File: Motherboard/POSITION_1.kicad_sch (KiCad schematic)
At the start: 28 parts, among them Q1 MOSFET_N_(DMN61D8LQ-13), Q3 MOSFET_N_(ZVN3320FTA)

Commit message: Schematic ready.  Going to clean up directory now.
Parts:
- C13, C14, C15, C20, C21: footprint Capacitors_SMD:C_1206 -> Capacitor_SMD:C_1206_3216Metric
- CAL2: footprint (none) -> Smart_Tank:FEMALE_SPADE_QC_(TE_63969-1)
- CTRL_SHUNT_1, PUMP_SHUNT_1: footprint _GARRETTS_PARTS:SHUNT_(WSL40261L000FEA) -> Smart_Tank:SHUNT_(WSL40261L000FEA)
- D1, D15: footprint Diodes_SMD:SOD-123 -> Diode_SMD:D_SMA
- Q1: footprint Package_TO_SOT_SMD:SOT-23 -> Smart_Tank:SOT-23
- Q3: footprint TO_SOT_Packages_SMD:SOT-23 -> Smart_Tank:SOT-23
- R1, R17, R18, R47, R48, R5, R6, R7: footprint Resistors_SMD:R_1206 -> Resistor_SMD:R_1206_3216Metric
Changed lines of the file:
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@@
 			)
 		)
-		(property "Footprint" "TO_SOT_Packages_SMD:SOT-23"
+		(property "Footprint" "Smart_Tank:SOT-23"
 			(at 119.38 94.615 0)
 			(effects
@@
 			)
 		)
-		(property "Footprint" "Resistors_SMD:R_1206"
+		(property "Footprint" "Resistor_SMD:R_1206_3216Metric"
 			(at 101.6 92.202 90)
 			(effects
@@
 			)
 		)
-		(property "Footprint" "Resistors_SMD:R_1206"
+		(property "Footprint" "Resistor_SMD:R_1206_3216Metric"
 			(at 117.348 81.28 90)
 			(effects
@@
 			)
 		)
-		(property "Footprint" "Resistors_SMD:R_1206"
+		(property "Footprint" "Resistor_SMD:R_1206_3216Metric"
 			(at 94.488 99.06 90)
 			(effects
@@
 			)
 		)
-		(property "Footprint" "Resistors_SMD:R_1206"
+		(property "Footprint" "Resistor_SMD:R_1206_3216Metric"
 			(at 85.09 153.162 90)
 			(effects
@@
 			)
 		)
-		(property "Footprint" "Resistors_SMD:R_1206"
+		(property "Footprint" "Resistor_SMD:R_1206_3216Metric"
 			(at 95.758 160.02 90)
 			(effects
@@
 			)
 		)
-		(property "Footprint" "Capacitors_SMD:C_1206"
+		(property "Footprint" "Capacitor_SMD:C_1206_3216Metric"
 			(at 229.5652 53.34 0)
 			(effects
@@
 			)
 		)
-		(property "Footprint" "Capacitors_SMD:C_1206"
+		(property "Footprint" "Capacitor_SMD:C_1206_3216Metric"
 			(at 219.4052 53.34 0)
 			(effects
@@
 			)
 		)
-		(property "Footprint" "Capacitors_SMD:C_1206"
+		(property "Footprint" "Capacitor_SMD:C_1206_3216Metric"
 			(at 229.5652 139.7 0)
 			(effects
@@
 			)
 		)
-		(property "Footprint" "Capacitors_SMD:C_1206"
+		(property "Footprint" "Capacitor_SMD:C_1206_3216Metric"
 			(at 219.4052 139.7 0)
 			(effects
@@
 			)
 		)
-		(property "Footprint" "Resistors_SMD:R_1206"
+		(property "Footprint" "Resistor_SMD:R_1206_3216Metric"
 			(at 185.928 86.36 90)
 			(effects
@@
 			)
 		)
-		(property "Footprint" "Resistors_SMD:R_1206"
+		(property "Footprint" "Resistor_SMD:R_1206_3216Metric"
 			(at 190.5 78.232 90)
 			(effects
@@
 			)
 		)
-		(property "Footprint" "Diodes_SMD:SOD-123"
+		(property "Footprint" "Diode_SMD:D_SMA"
 			(at 237.49 80.01 0)
 			(effects
@@
 			)
 		)
-		(property "Footprint" "Capacitors_SMD:C_1206"
+		(property "Footprint" "Capacitor_SMD:C_1206_3216Metric"
 			(at 257.81 48.5648 0)
 			(effects
@@
 			)
 		)
-		(property "Footprint" "Resistors_SMD:R_1206"
+		(property "Footprint" "Resistor_SMD:R_1206_3216Metric"
 			(at 74.168 43.18 90)
 			(effects
@@
 			)
 		)
-		(property "Footprint" "Package_TO_SOT_SMD:SOT-23"
+		(property "Footprint" "Smart_Tank:SOT-23"
 			(at 118.11 134.62 0)
 			(effects
@@
 			)
 		)
-		(property "Footprint" ""
+		(property "Footprint" "Smart_Tank:FEMALE_SPADE_QC_(TE_63969-1)"
 			(at 254 33.02 0)
 			(effects
@@
 			)
 		)
-		(property "Footprint" "Diodes_SMD:SOD-123"
+		(property "Footprint" "Diode_SMD:D_SMA"
 			(at 254 41.91 0)
 			(effects
@@
 			)
 		)
-		(property "Footprint" "_GARRETTS_PARTS:SHUNT_(WSL40261L000FEA)"
+		(property "Footprint" "Smart_Tank:SHUNT_(WSL40261L000FEA)"
 			(at 195.58 53.848 90)
 			(effects
@@
 			)
 		)
-		(property "Footprint" "_GARRETTS_PARTS:SHUNT_(WSL40261L000FEA)"
+		(property "Footprint" "Smart_Tank:SHUNT_(WSL40261L000FEA)"
 			(at 195.58 140.208 90)
 			(effects

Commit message: Started cleaning out old parts from PCB.
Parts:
- PUMP_V_CONN_1: footprint Smart_Tank:PHNX_TB_SCREW_4_POS_(1729144) -> Smart_Tank:PHX_TB_HDR_4_POS_STR_(1755752)
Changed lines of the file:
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@@
 			)
 		)
-		(property "Footprint" "Smart_Tank:PHNX_TB_SCREW_4_POS_(1729144)"
+		(property "Footprint" "Smart_Tank:PHX_TB_HDR_4_POS_STR_(1755752)"
 			(at 250.19 83.82 0)
 			(effects

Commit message: Continued cleanup and reconnects.
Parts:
- Q1, Q3: footprint Smart_Tank:SOT-23 -> Package_TO_SOT_SMD:SOT-23
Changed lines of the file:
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@@
 			)
 		)
-		(property "Footprint" "Smart_Tank:SOT-23"
+		(property "Footprint" "Package_TO_SOT_SMD:SOT-23"
 			(at 119.38 94.615 0)
 			(effects
@@
 			)
 		)
-		(property "Footprint" "Smart_Tank:SOT-23"
+		(property "Footprint" "Package_TO_SOT_SMD:SOT-23"
 			(at 118.11 134.62 0)
 			(effects

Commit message: Almost done with re-routing.
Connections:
- net POS_1_SPARE renamed POS_1_SPR_1
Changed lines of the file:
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@@
 		)
 	)
-	(global_label "POS_1_SPARE"
+	(global_label "POS_1_SPR_1"
 		(shape input)
 		(at 58.42 59.69 0)

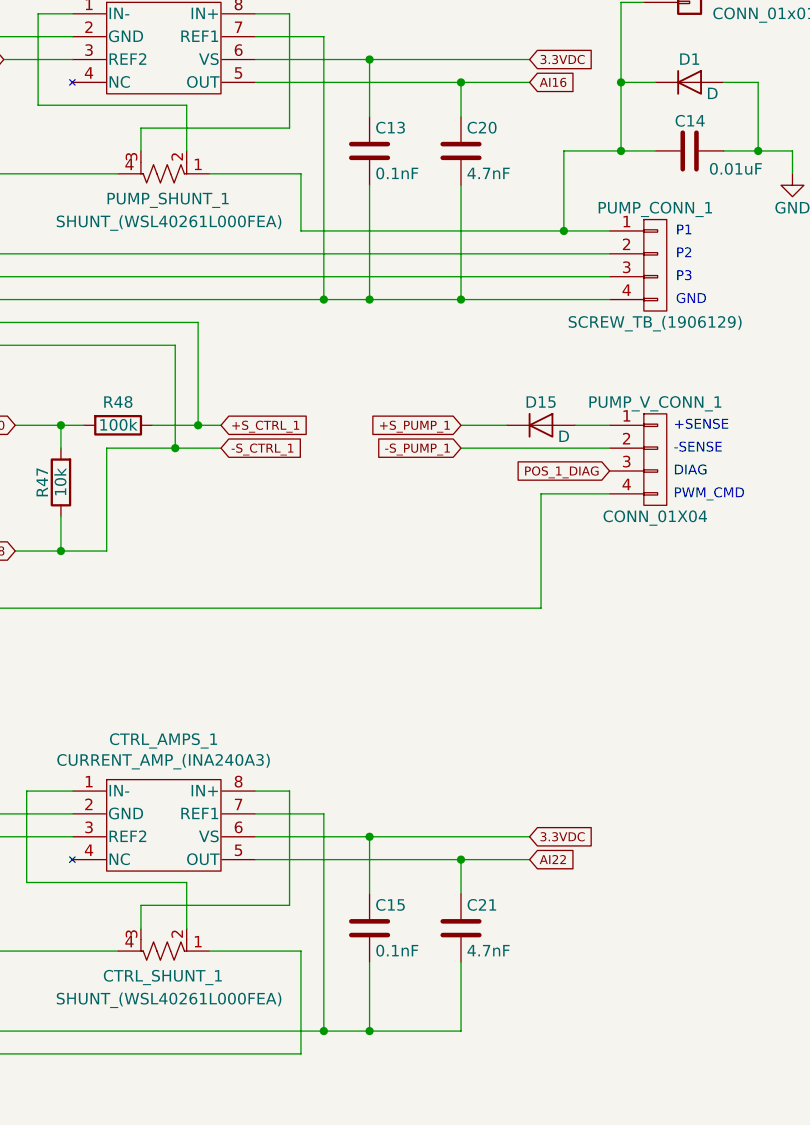
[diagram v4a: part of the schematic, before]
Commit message: Capacitor part issues...
Made these changes...

Concerning C13, C15, C27, C28, C31, C32, C35, C36, C39, C40, C43, C44
The schematic is wrong, and the BOM is correct.  These should all be 0.1uF
Concerning C20, C21, C29, C30, C33, C34, C37, C38, C41, C42, C45, C46
The BOM is wrong, and the schematic is correct.  These should all be 4.7nF
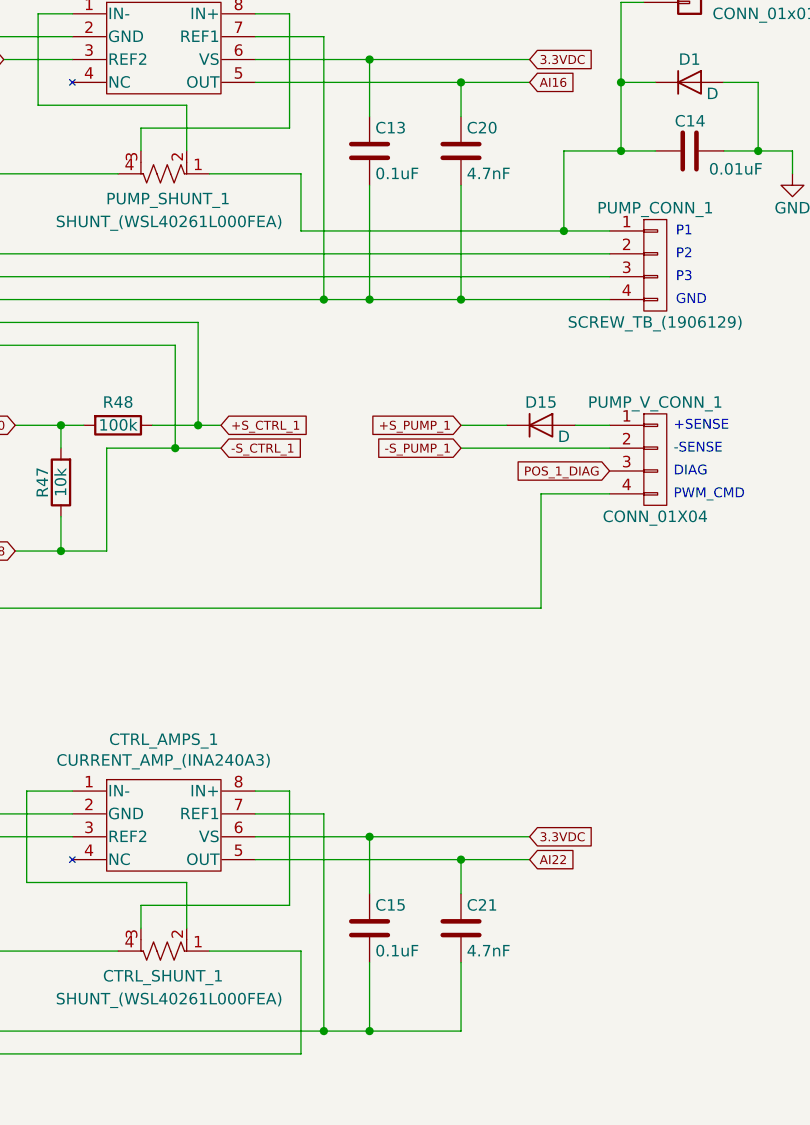
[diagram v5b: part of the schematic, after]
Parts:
- C13, C15: value 0.1nF -> 0.1uF
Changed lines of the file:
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@@
 			)
 		)
-		(property "Value" "0.1nF"
+		(property "Value" "0.1uF"
 			(at 219.075 52.07 0)
 			(effects
@@
 			)
 		)
-		(property "Value" "0.1nF"
+		(property "Value" "0.1uF"
 			(at 219.075 138.43 0)
 			(effects
